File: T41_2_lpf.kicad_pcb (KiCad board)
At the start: 2 copper layers, 100 x 100 mm, 116 parts, among them J1 5-1814832-1, J2 5-1814832-1, J3 5-1814832-1, J4 Conn_02x08_Odd_Even, J5 Conn_02x05_Odd_Even, J6 B2B-XH-A_LF__SN_, Q1 Q_NMOS_GSD, Q2 Q_NMOS_GSD, Q3 Q_NMOS_GSD, Q4 Q_NMOS_GSD, Q5 Q_NMOS_GSD, Q6 Q_NMOS_GSD, U12 4002, U13 TCA9534

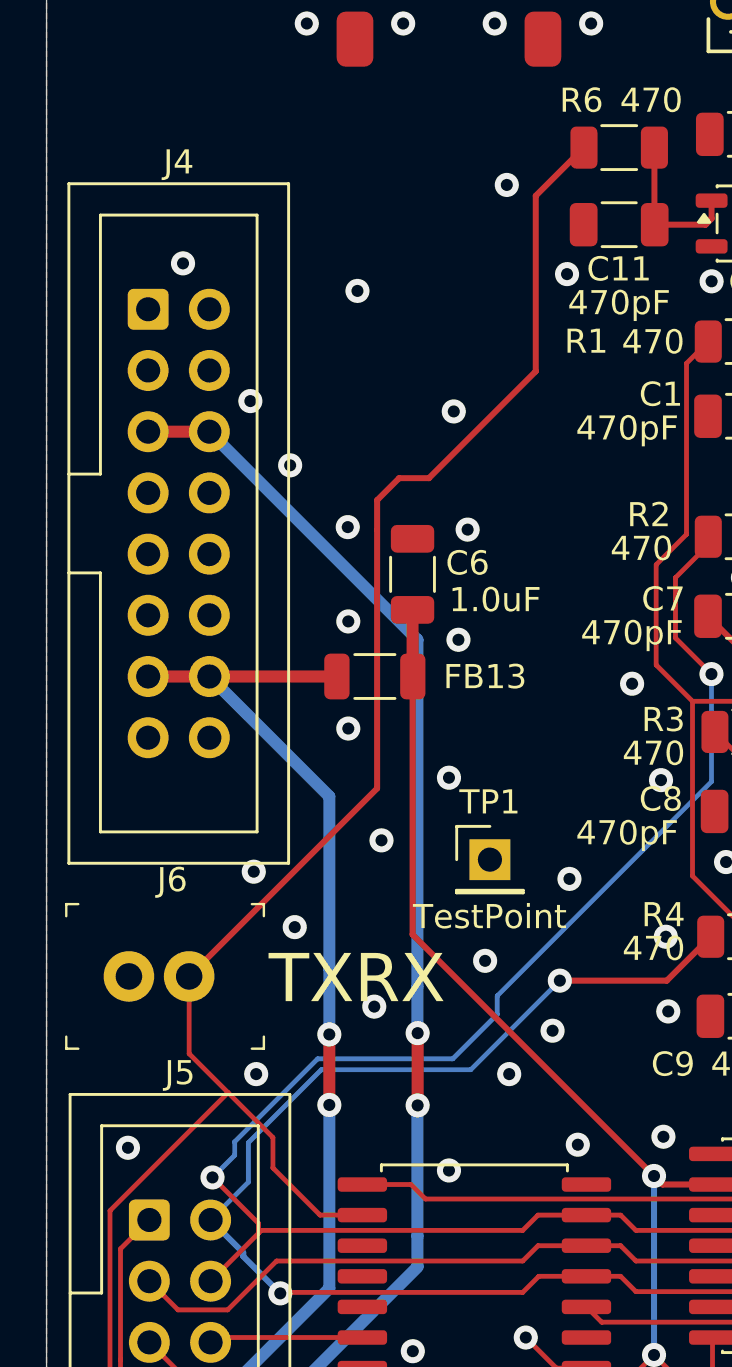
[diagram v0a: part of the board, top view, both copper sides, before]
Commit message: Added bypass capacitor to TXRX.  Did not uprev.
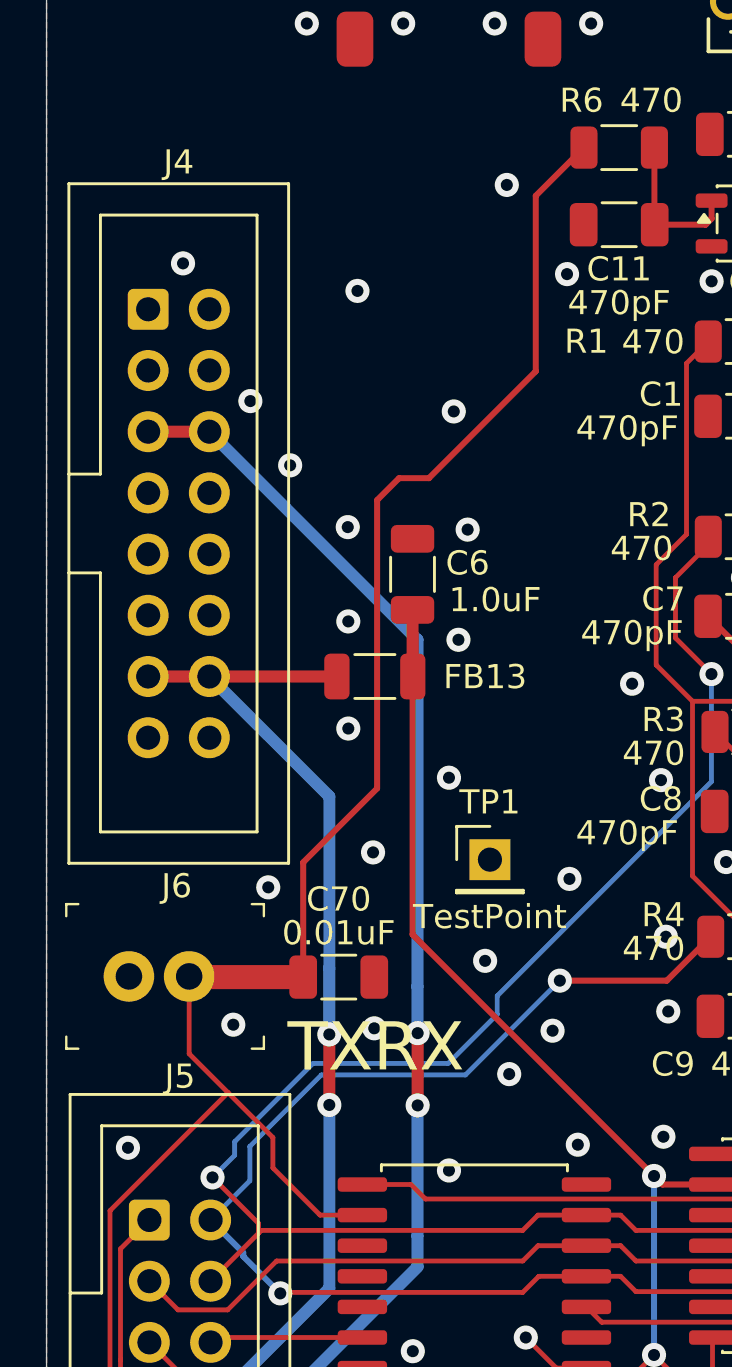
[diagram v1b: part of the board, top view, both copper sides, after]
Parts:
- added C70: 0.01uF, Capacitor_SMD:C_1206_3216Metric, F.Cu at (112.1, 114.1)
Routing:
- net /TXRX: track 79.7 -> 82.5 mm
- net GND: vias 226 -> 225
